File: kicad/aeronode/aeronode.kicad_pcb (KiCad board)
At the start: 4 copper layers, 90 x 70 mm, 77 parts, among them J1 IMU_BOARD, J2 USB-C PD / recovery, J3 2S LiFePO4 6Ah + BMS, Q1 NMOS pass - TBD, SW1 ON/OFF, U1 ConnectCore93_LGA, U10 BMP390, U2 CYPD3177-24LQ, U3 BQ25798, U4 LMR33630ADDA, U5 LTC4364CMS, U6 BME690, U7 DAN-F10N, U9 MMC5983MA

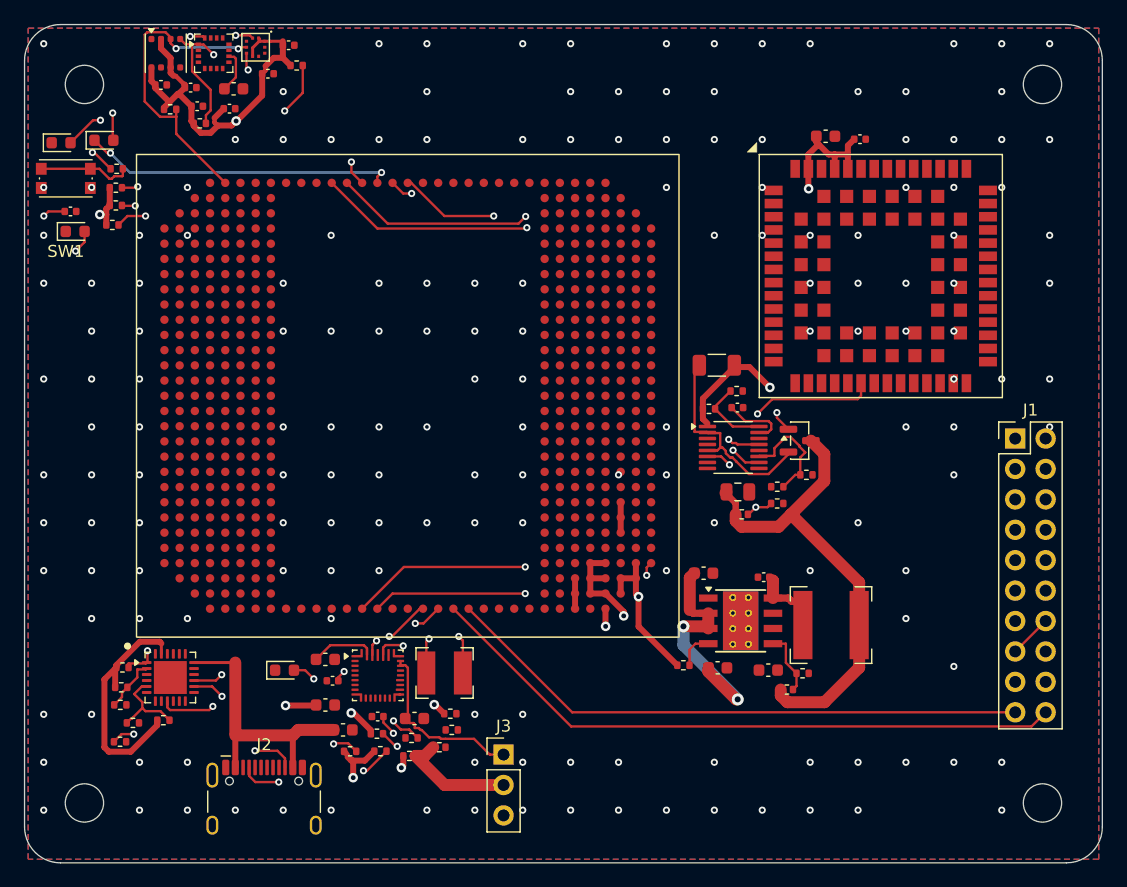
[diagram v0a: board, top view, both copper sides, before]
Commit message: [LIMA] kicad: narrow signal tracks to 0.125mm - unconnected 59->37, DRC 0
Peter's suggestion to narrow the tracks was right and the effect is large.
Narrowed ONLY the Default class to 0.125mm/0.125mm (5/5 mil), via 0.45-0.25.
Power (0.5mm) and HighCurrent (1.0mm) deliberately unchanged so the 3A charger
path keeps its width - narrowing that would trade routing for thermal risk.

                        0.20mm      0.125mm
  unrouted pass 1         56          36
  unrouted final          41          18
  router wall time      87 min      12.5 min
  KiCad unconnected       59          37
  signal nets unconn.    ~25           3

The narrowed run beat the previous run's best 24-pass result on its first pass
and finished 7x faster. Geometry verified before committing: CC93 LGA pads on
1.27mm pitch leave 0.570mm; a 0.125mm track with clearance needs 0.425mm.

Fixed a self-inflicted inconsistency: Default clearance 0.15mm against a board
minimum of 0.125mm. Freerouting honoured the board rule, KiCad checked the class
rule, producing two phantom violations at U6. Class and board minimum must agree.

Remaining 37: 19 are /GND pour-region-to-pour-region, NOT missing tracks - pour
regions holding a GND pad but no via to the In1 plane. Placing vias there failed
(0 of 36 at 0.32mm margin, 4 of 36 at 0.22mm) and made things worse, so it was
reverted. Too tight for a 0.5mm via; needs hand work or a different zone
strategy. 13 are power nets that must stay wide, 3 are signals.

Fab note: 0.10mm annular ring and 5/5 mil trace/space - standard but fine.
Also gitignored KiCad's ~*.lck editor lock files.

Co-Authored-By: Claude Opus 5 <noreply@anthropic.com>
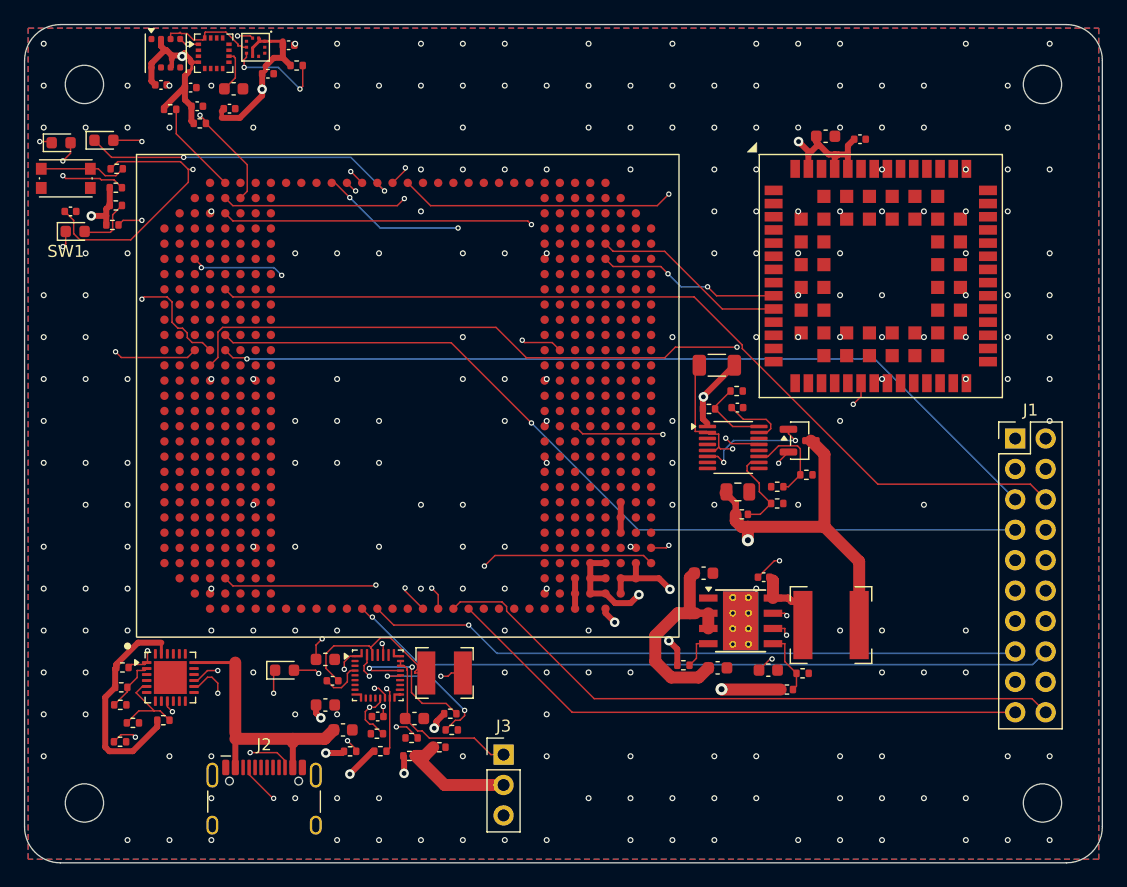
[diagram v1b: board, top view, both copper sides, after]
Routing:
- net /BMI_GYR_CS: track 0.00 -> 84.4 mm, vias 0 -> 2
- net /ICM_INT2: track 0.00 -> 81.4 mm, vias 0 -> 1
- net /ICM_INT1: track 0.00 -> 79.0 mm, vias 0 -> 1
- net /ICM_MISO: track 0.00 -> 75.9 mm
- net /ICM_SCLK: track 0.00 -> 75.4 mm, vias 0 -> 1
- net /ICM_CS: track 0.00 -> 72.7 mm, vias 0 -> 1
- net /ICM_MOSI: track 0.00 -> 71.1 mm, vias 0 -> 1
- net /ON_OFF_N: track 11.0 -> 59.8 mm
- net /CHG_INT_N: track 0.00 -> 33.2 mm, vias 0 -> 3
- net /LED_RED_N: track 0.00 -> 28.3 mm, vias 0 -> 2
- net /SD_VSELECT: track 0.00 -> 18.7 mm, vias 0 -> 2
- net /LED_GRN_N: track 0.00 -> 18.6 mm, vias 0 -> 2
- net /GNSS_TXD: track 0.00 -> 16.3 mm
- net /GNSS_RXD: track 0.00 -> 15.3 mm, vias 0 -> 2
- net /I2C4_SDA: track 29.0 -> 16.1 mm, vias 3 -> 0
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
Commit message: [LIMA] kicad: rework stackup to SIG/GND/PWR/SIG per request - DRC 0
In1 = solid GND plane, In2 = voltage planes only, F/B = signal routing.
Previously In2 was typed 'signal' and carried 108 signal tracks straight across
the power layer; those are gone and In2 is rebuilt as a multi-rail plane:
+3V3 4859mm2, +5V_RAW 412, VBUS 246, +5V 236. Regions derived from measured pad
clusters; overlaps resolved by zone priority, highest current first.

811 tracks (2045mm), 380 vias, DRC 0 violations, parity 0, unconnected 53.

The cost, stated plainly: 37 unconnected with signals allowed on In2 vs 53 with
the clean stackup. That is the right trade - each of those 108 tracks was a slot
cut in the +3V3 plane and a break in its return path, on a board carrying a GNSS
receiver and a magnetometer.

Removed the VSYS_CHG plane deliberately: it held a fill with a pad but no via,
giving a persistent isolated_copper violation, and with 5 pads on a short hop in
the most congested corner a plane was never worth it. The router already carries
it on 1.0mm HighCurrent tracks. That took DRC to 0.

VBUS fanout initially failed 9 of 9 using 0.8mm vias in the USB-C corner, leaving
its plane entirely isolated. Retried at 0.6/0.3 and placed 4. Oversized vias in
congested areas fail silently and strand a whole plane.

API note: ZONE.SetMinThermalReliefSpokeCount does not exist; spoke count is the
board setting min_resolved_spokes (set to 1 for J1's PTH pads).

Still open: 36 of 53 unconnected are /GND pour-region items needing hand work.

Co-Authored-By: Claude Opus 5 <noreply@anthropic.com>
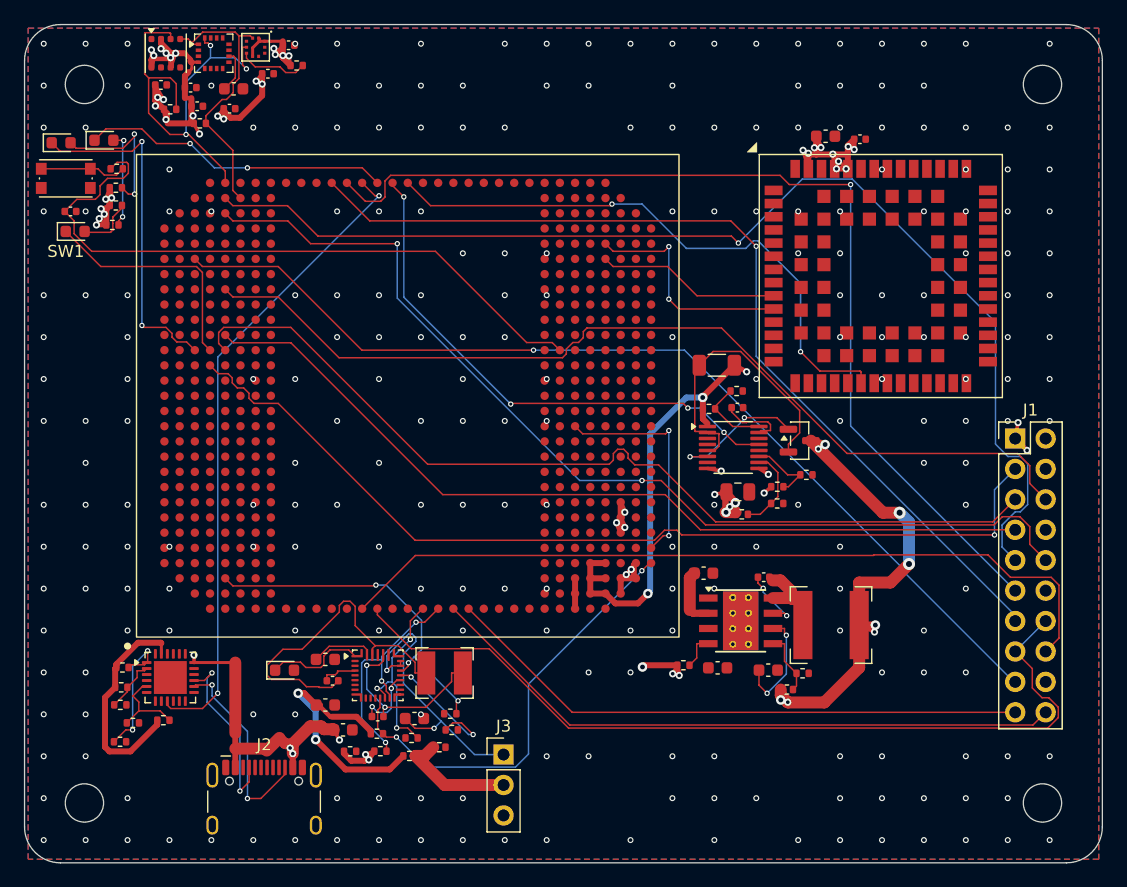
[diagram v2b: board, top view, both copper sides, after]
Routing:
- net /+3V3: track 65.3 -> 100.1 mm, vias 10 -> 45
- net /I2C4_SDA: track 16.1 -> 38.5 mm, vias 0 -> 3
- net /ICM_INT1: track 79.0 -> 96.2 mm
- net /BMI_SDO: track 58.5 -> 72.6 mm, vias 1 -> 0
- net /CHG_SW1: track 14.3 -> 28.1 mm
- net /VSYS_CHG: track 17.5 -> 4.89 mm
- net /VBAT: track 14.8 -> 24.9 mm, vias 0 -> 2
- net /CHG_LED_A: track 9.98 -> 0.51 mm, vias 2 -> 0
- net /REGN: track 12.0 -> 21.0 mm
- net /OVP_SENSE: track 16.7 -> 24.7 mm, vias 2 -> 0
- net /BMI_ACC_CS: track 59.5 -> 67.1 mm, vias 1 -> 0
- net /ICM_MOSI: track 71.1 -> 77.5 mm, vias 1 -> 0
- net /CHG_BTST2: track 0.00 -> 5.58 mm, vias 0 -> 2
- net /VBUS: track 23.1 -> 28.2 mm, vias 0 -> 4
- net /+5V: track 37.4 -> 42.4 mm, vias 2 -> 6
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- added copper zone on In2.Cu, net /+5V
- added copper zone on In2.Cu, net /+5V_RAW
- added copper zone on In2.Cu, net /VBUS
